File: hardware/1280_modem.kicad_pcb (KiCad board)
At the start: 4 copper layers, 38 x 53 mm, 73 parts, among them IC1 SX1281IMLTRT, IC2 SKY65383-11, IC3 TJA1462AT_0Z, J1 jst_sh 6, J2 Conn_Coaxial, J3 USB_C_Receptacle_USB2.0, J4 jst gh 4, J5 jst gh 6, U1 STM32U575CGTx, U2 TPS7A20285PDBVR, U3 USBLC6-2SC6, Y1 48MHz, Y2 52MHz

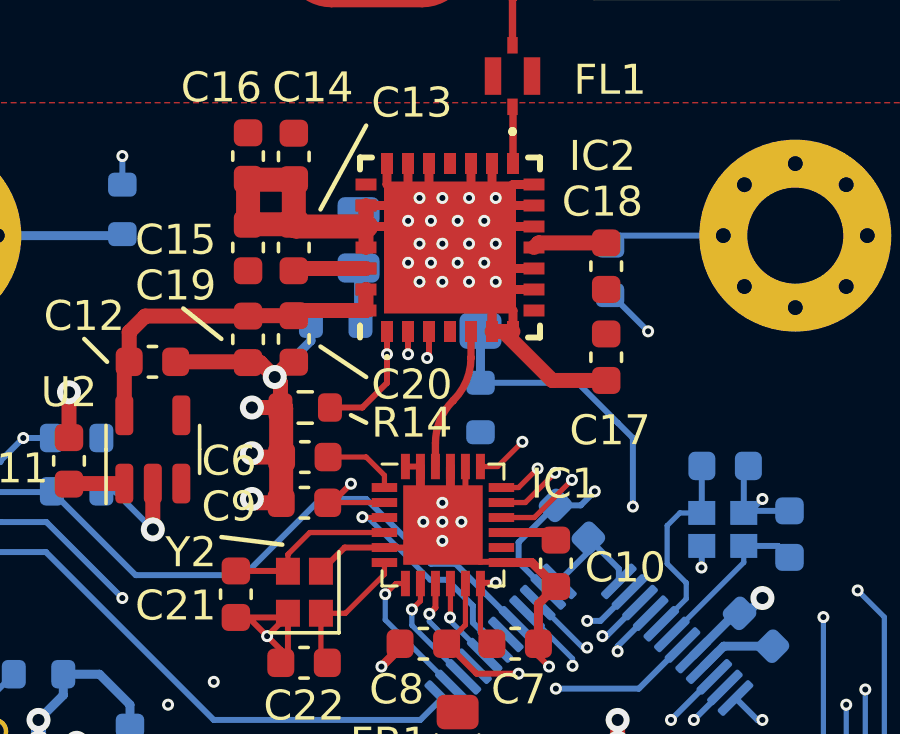
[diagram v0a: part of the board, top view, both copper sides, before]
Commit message: prettier thermal vias
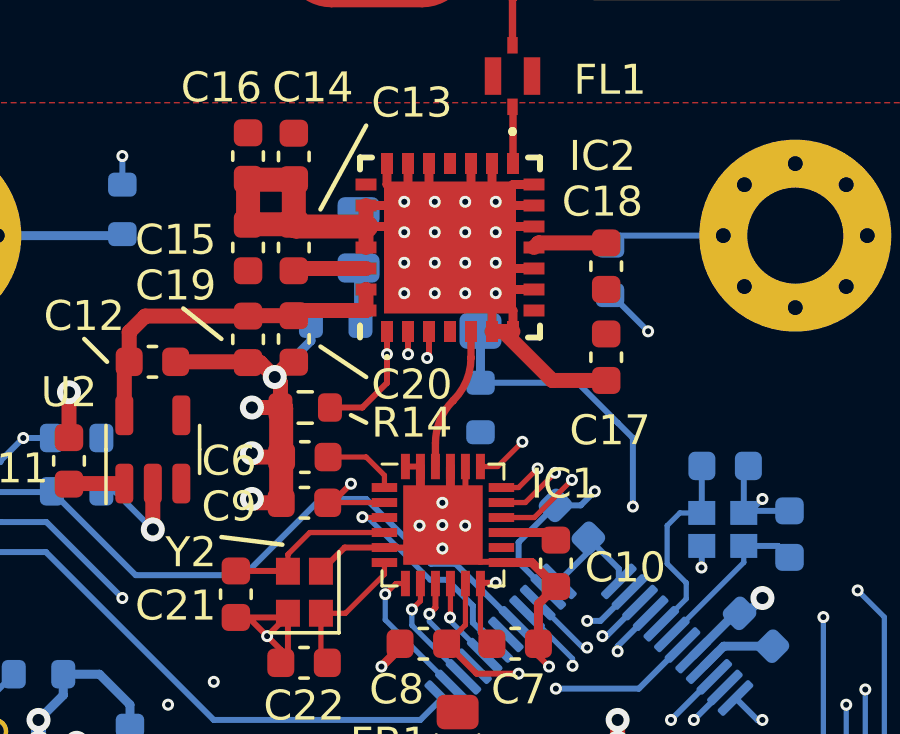
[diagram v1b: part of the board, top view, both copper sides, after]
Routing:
- net Earth: track 179.0 -> 180.1 mm, vias 82 -> 78

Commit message: improvements
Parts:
- added C30: 1u, Capacitor_SMD:C_0603_1608Metric, F.Cu at (91.5, 79.3)
- added C31: 1u, Capacitor_SMD:C_0603_1608Metric, F.Cu at (94.6, 76.0)
- added D4: MBR1020VL, Diode_SMD:D_SOD-323_HandSoldering, F.Cu at (95.5, 78.5)
- added D5: SZNUP2105L, Package_TO_SOT_SMD:SOT-23, F.Cu at (101.4, 85.6)
- added D6: SZNUP2105L, Package_TO_SOT_SMD:SOT-23, F.Cu at (114.3, 90.7)
- added D7: SZNUP2105L, Package_TO_SOT_SMD:SOT-23, F.Cu at (110.2, 90.7)
- added D8: SZNUP2105L, Package_TO_SOT_SMD:SOT-23, F.Cu at (106.0, 88.5)
- added G***: LOGO, LOGO, F.Cu at (98.9, 52.8)
- added G***: LOGO, LOGO, B.Cu at (102.2, 43.4)
- added G***: LOGO, LOGO, B.Cu at (99.6, 52.7)
- added JP1: SolderJumper_2_Open, Jumper:SolderJumper-2_P1.3mm_Open_TrianglePad1.0x1.5mm, F.Cu at (100.5, 90.3)
- added U4: TPS7A2450DBVR, Package_TO_SOT_SMD:SOT-23-5, F.Cu at (91.2, 76.5)
- moved R15 10.2 mm to (124.2, 63.5)
- moved R13 8.53 mm to (115.2, 60.1)
- moved D3 8.41 mm to (115.8, 57.3)
- moved R16 7.82 mm to (93.9, 50.3), turned to 180 degrees
- moved R18 5.70 mm to (102.6, 90.2), turned to -90 degrees
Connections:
- C23 pad 1: +5V -> VCC
- C24 pad 2: +5V -> VCC
- J3 pad A4: +5V -> /VBUS
- J3 pad A9: +5V -> /VBUS
- J3 pad B4: +5V -> /VBUS
- J3 pad B9: +5V -> /VBUS
- J4 pad 1: +5V -> VCC
- J5 pad 1: +5V -> VCC
- PS1 pad 1: +5V -> VCC
- PS1 pad 2: +5V -> VCC
- PS1 pad 3: +5V -> VCC
- R18 pad 2: /CAN_L -> Net-(JP1-A)
- U3 pad 5: +5V -> /VBUS
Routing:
- net VCC: track 0.00 -> 42.3 mm, vias 0 -> 6
- net /VBUS: track 0.00 -> 22.4 mm, vias 0 -> 5
- net +5V: track 38.9 -> 23.3 mm, vias 10 -> 2
- net Earth: track 180.1 -> 184.6 mm, vias 78 -> 81
- net /UART_RX: track 19.9 -> 22.2 mm
- net /UART_CTS: track 22.0 -> 24.2 mm
- net Net-(JP1-A): track 0.00 -> 2.18 mm
- net /CAN_L: track 5.87 -> 7.92 mm
- net /UART_TX: track 21.2 -> 23.1 mm
- net /UART_RTS: track 20.4 -> 22.4 mm
- net /CAN_H: track 5.87 -> 7.63 mm
- net Net-(H1-Pad1): track 6.31 -> 7.09 mm
- added copper zone on F.Cu, net VCC
- removed copper zone on F.Cu, net +5V
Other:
- board text added: "BRAGE"
- board text added: "V1.0 NOV 2023"

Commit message: stuff
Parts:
- removed D3: pwr, LED_SMD:LED_0805_2012Metric
- removed R13: 330, Resistor_SMD:R_0603_1608Metric
- added D9: IN-S128TATRGB, LED_SMD:LED_RGB_1210, B.Cu at (115.7, 58.2)
- added R19: 330, Resistor_SMD:R_0603_1608Metric, B.Cu at (115.7, 62.0)
- moved G*** 16.4 mm to (96.8, 69.1)
- moved R16 13.3 mm to (101.2, 61.3)
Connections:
- U1 pad 20: unconnected-(U1-PB2-Pad20) -> /LED_G
- U1 pad 27: unconnected-(U1-PB14-Pad27) -> /LED_B
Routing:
- net /LED_G: track 0.00 -> 53.6 mm, vias 0 -> 2
- net /LED_B: track 0.00 -> 46.7 mm, vias 0 -> 2
- net +3V3: track 43.5 -> 47.0 mm
- net Net-(H2-Pad1): track 6.22 -> 9.40 mm
- net Net-(D9-A): track 0.00 -> 2.69 mm
- net Net-(D3-K): track 1.94 -> 0.00 mm
- net /THERM: track 30.2 -> 29.1 mm
- net Earth: track 184.6 -> 185.6 mm, vias 81 -> 80

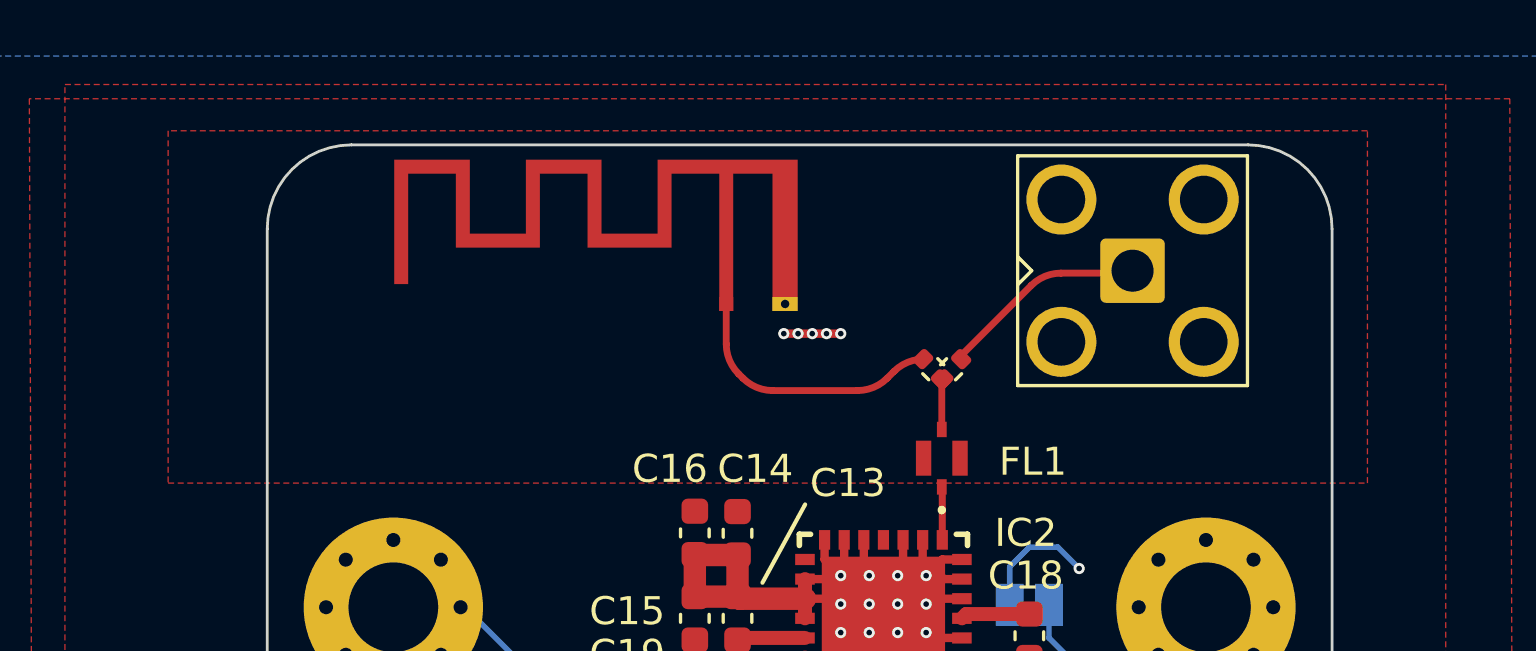
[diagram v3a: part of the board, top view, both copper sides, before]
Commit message: micro strip and antenna tuning
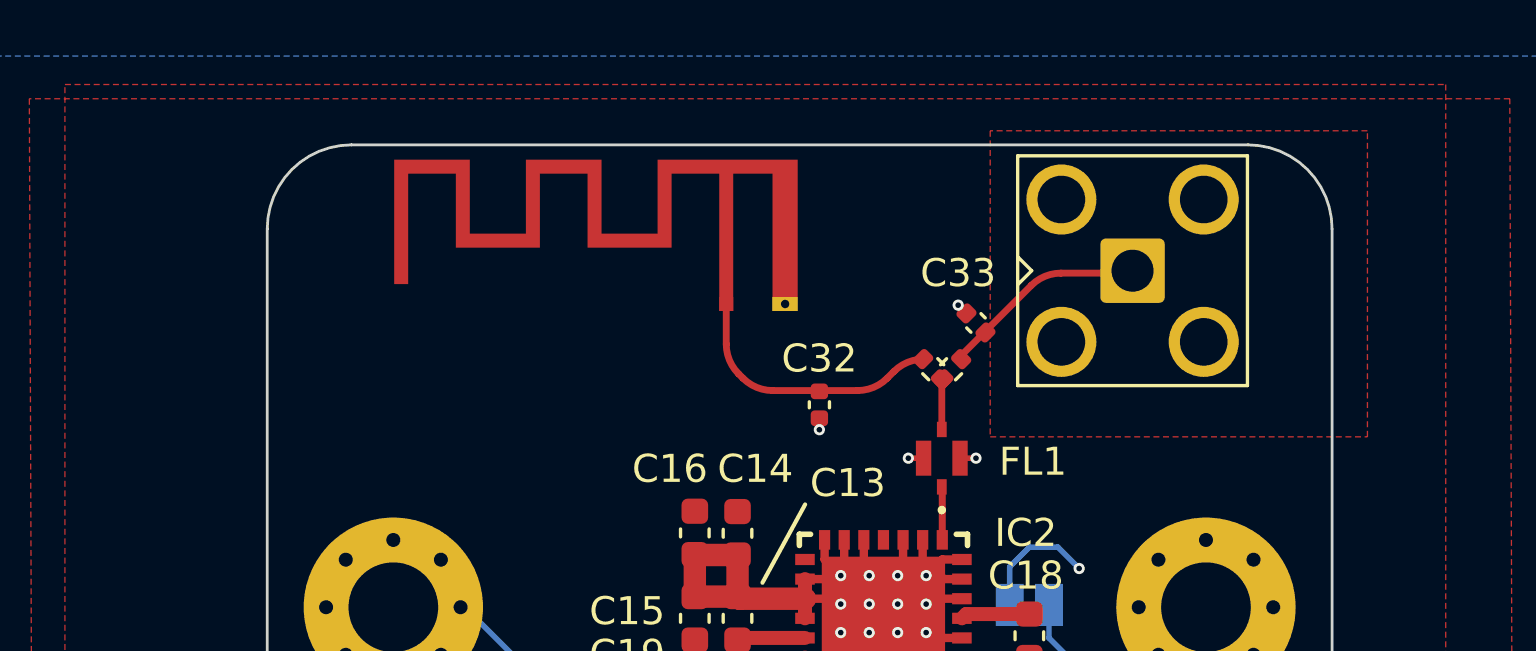
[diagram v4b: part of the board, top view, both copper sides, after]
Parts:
- added C32: TBD, Capacitor_SMD:C_0402_1005Metric, F.Cu at (108.2, 49.3)
- added C33: TBD, Capacitor_SMD:C_0402_1005Metric, F.Cu at (113.8, 46.4)
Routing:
- net Earth: track 185.6 -> 185.5 mm, vias 80 -> 79

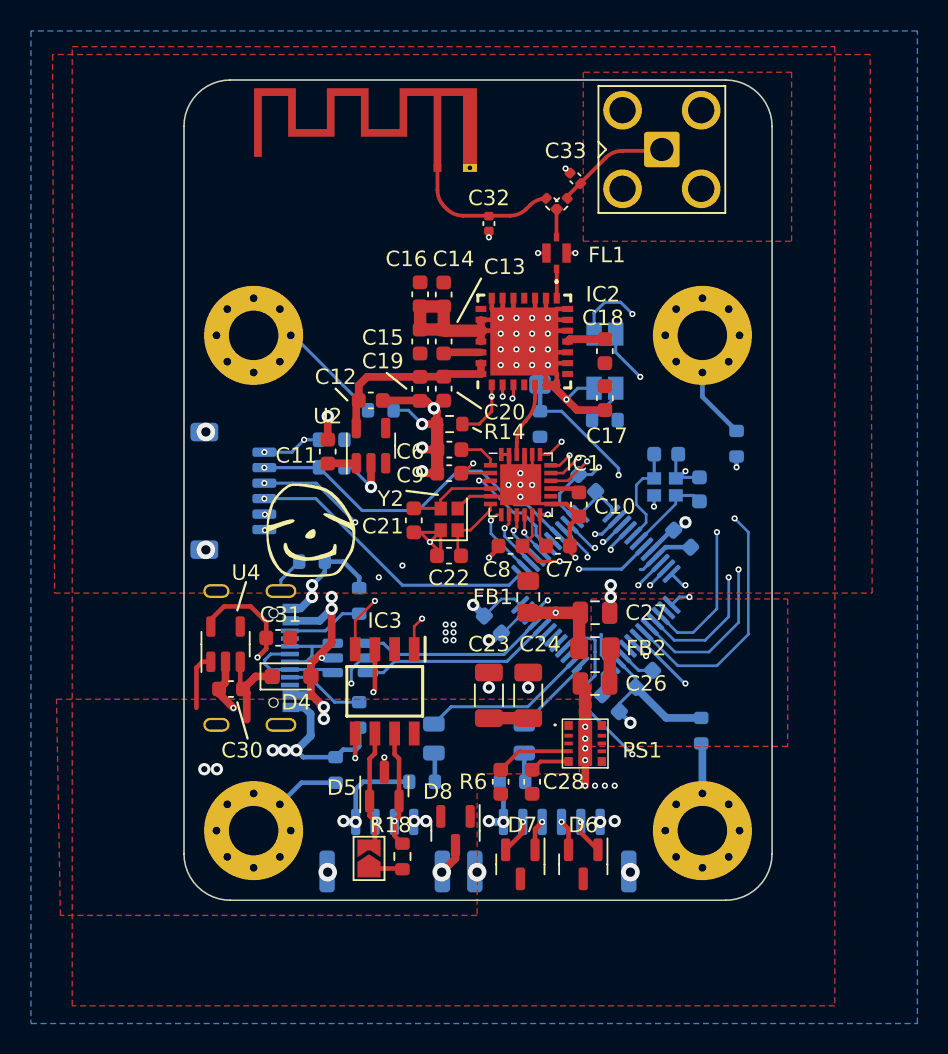
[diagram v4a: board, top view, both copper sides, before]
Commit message: better power electronics
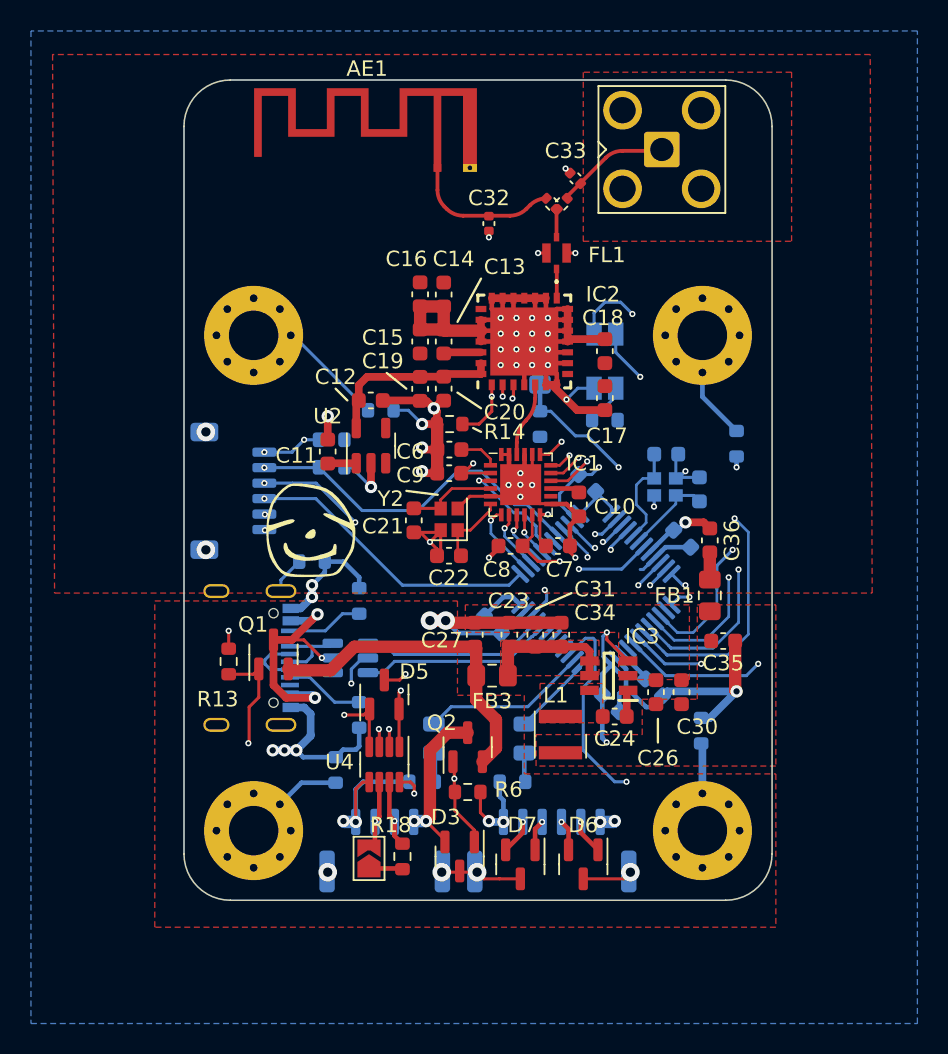
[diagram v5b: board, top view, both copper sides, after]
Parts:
- removed C28: 4u7, Capacitor_SMD:C_0603_1608Metric
- removed D4: MBR1020VL, Diode_SMD:D_SOD-323_HandSoldering
- removed D8: SZNUP2105L, Package_TO_SOT_SMD:SOT-23
- removed FB2: BLM18KG102SN1D, Inductor_SMD:L_0805_2012Metric_Pad1.15x1.40mm_HandSolder
- removed PS1: TPSM82901SISR, tpsm82901:TPSM82901SISR
- added C34: 100n, Capacitor_SMD:C_0603_1608Metric, F.Cu at (112.9, 75.8)
- added C35: 1u, Capacitor_SMD:C_0603_1608Metric, F.Cu at (123.3, 76.3)
- added C36: 1u, Capacitor_SMD:C_0603_1608Metric, F.Cu at (122.5, 69.7)
- added D3: SZNUP2105L, Package_TO_SOT_SMD:SOT-23, F.Cu at (106.3, 90.2)
- added FB3: BLM18KG102SN1D, Inductor_SMD:L_0805_2012Metric_Pad1.15x1.40mm_HandSolder, F.Cu at (108.4, 78.5)
- added L1: 4.7u, Inductor_SMD_Wurth:L_Wurth_WE-LQSH-3012, F.Cu at (112.8, 82.3)
- added Q1: AO3401A, Package_TO_SOT_SMD:SOT-23, F.Cu at (94.3, 77.1)
- added Q2: AO3401A, Package_TO_SOT_SMD:SOT-23, F.Cu at (106.8, 83.1)
- added R13: 10k, Resistor_SMD:R_0603_1608Metric, F.Cu at (91.4, 77.6)
- C23: value 10u -> 1u; footprint Capacitor_SMD:C_1206_3216Metric -> Capacitor_SMD:C_0603_1608Metric
- C24: value 10u -> 100n; footprint Capacitor_SMD:C_1206_3216Metric -> Capacitor_SMD:C_0603_1608Metric
- C26, C27: value 22u -> 10u; footprint Capacitor_SMD:C_0805_2012Metric -> Capacitor_SMD:C_0603_1608Metric
- C30: value 1u -> 10u
- IC3: value TJA1462AT_0Z -> LMR50410Y3; footprint tja1462:SOIC127P600X175-8N -> lmr50410:SOT95P280X145-6N
- R6: value 26k1 -> 10k; footprint Capacitor_SMD:C_0603_1608Metric -> Resistor_SMD:R_0603_1608Metric
- U4: value TPS7A2450DBVR -> TCAN334; footprint Package_TO_SOT_SMD:SOT-23-5 -> Package_TO_SOT_SMD:TSOT-23-8
- moved C30 29.1 mm to (120.7, 79.6), turned to 90 degrees
- moved C31 16.6 mm to (111.2, 75.8), turned to -90 degrees
- moved IC3 14.5 mm to (116.0, 78.5), turned to 180 degrees
- moved U4 12.9 mm to (101.4, 84.2), turned to -90 degrees
- moved FB1 11.7 mm to (122.5, 73.3)
- moved C24 8.24 mm to (116.3, 81.1), turned to 180 degrees
- moved C27 7.90 mm to (107.3, 75.8), turned to -90 degrees
- moved D5 5.94 mm to (101.4, 79.7)
- moved C23 4.10 mm to (109.5, 75.8), turned to -90 degrees
- moved C26 3.98 mm to (119.0, 79.6), turned to 90 degrees
- moved R6 2.23 mm to (106.8, 86.0), turned to 180 degrees
- moved C1 0.84 mm to (118.9, 79.2), turned to 135 degrees
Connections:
- C23 pad 1: VCC -> Earth
- C23 pad 2: Earth -> /VCC_FILT
- C24 pad 1: Earth -> /CB
- C24 pad 2: VCC -> /SW
- C26 pad 1: /3v3_raw -> +3V3
- C27 pad 1: +3V3 -> Earth
- C27 pad 2: Earth -> VCC
- C30 pad 1: Earth -> +3V3
- C30 pad 2: VCC -> Earth
- C31 pad 1: +5V -> Earth
- C31 pad 2: Earth -> /VCC_FILT
- D5 pad 1: /CAN_L -> /CAN_RX
- D5 pad 2: /CAN_H -> /CAN_TX
- IC3 pad 1: /CAN_TX -> /CB
- IC3 pad 3: +5V -> +3V3
- IC3 pad 4: /CAN_RX -> /VCC_FILT
- IC3 pad 5: +3V3 -> /VCC_FILT
- IC3 pad 6: /CAN_L -> /SW
- J3 pad A4: /VBUS -> /VUSB
- J3 pad A9: /VBUS -> /VUSB
- J3 pad B4: /VBUS -> /VUSB
- J3 pad B9: /VBUS -> /VUSB
- J4 pad 1: VCC -> /VPORT
- J5 pad 1: VCC -> /VPORT
- R6 pad 2: Net-(PS1-MODE/S-CONF) -> /VUSB
- U3 pad 5: /VBUS -> /VUSB
- U4 pad 1: VCC -> /CAN_TX
- U4 pad 3: VCC -> +3V3
- U4 pad 4: unconnected-(U4-NC-Pad4) -> /CAN_RX
- U4 pad 5: +5V -> Earth
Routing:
- net /VPORT: track 0.00 -> 50.2 mm, vias 0 -> 5
- net Earth: track 185.5 -> 220.8 mm, vias 79 -> 64
- net /VUSB: track 0.00 -> 33.1 mm, vias 0 -> 4
- net +5V: track 23.3 -> 0.00 mm, vias 2 -> 0
- net /VBUS: track 22.4 -> 0.00 mm, vias 5 -> 0
- net VCC: track 42.3 -> 21.1 mm, vias 6 -> 0
- net +3V3: track 47.0 -> 27.1 mm, vias 7 -> 5
- net /LED_G: track 53.6 -> 41.5 mm
- net /VCC_FILT: track 0.00 -> 8.78 mm
- net /SW_DIO: track 29.9 -> 23.1 mm
- net /CAN_RX: track 21.5 -> 27.4 mm
- net Net-(PS1-MODE/S-CONF): track 4.88 -> 0.00 mm
- net /CAN_TX: track 18.8 -> 23.4 mm
- net /LED_B: track 46.7 -> 51.0 mm
- net /CAN_L: track 7.92 -> 4.62 mm
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- added copper zone on F.Cu, net +3V3
- added copper zone on F.Cu, net /SW
- added copper zone on F.Cu, net /VCC_FILT
- removed copper zone on F.Cu, net /3v3_raw
- removed copper zone on F.Cu, net VCC

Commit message: bamse
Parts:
- added G***: LOGO, LOGO, F.Cu at (99.6, 75.4)
- added G***: LOGO, LOGO, F.Cu at (94.8, 47.5)
- added G***: LOGO, LOGO, F.Cu at (120.9, 63.8)
- added G***: LOGO, LOGO, F.Cu at (93.0, 66.3)
- G***: moved to B.Cu
- moved G*** 8.40 mm to (105.2, 68.6), turned to 180 degrees
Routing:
- net +3V3: track 27.1 -> 29.3 mm, vias 5 -> 7
- net /SW_DIO: track 23.1 -> 25.0 mm, vias 3 -> 2
- net /NRST: track 30.9 -> 31.9 mm
- net /VPORT: track 50.2 -> 51.0 mm
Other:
- board text added: "V1.0 FEB 2024"
- board text removed: "V1.0 NOV 2023"

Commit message: second pass
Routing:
- added copper zone on F.Cu, net VCC
